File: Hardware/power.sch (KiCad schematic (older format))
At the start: 0 parts

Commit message: add power jack, 3.3V regulator, VREF divider
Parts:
- added C?: 220uF, symbol CP1_Small
- added C?: 1uF, symbol CP1_Small
- added C?: 4.7uuF, symbol CP1_Small
- added D?: D, symbol D
- added J?: Barrel_Jack, symbol Barrel_Jack
- added R? (x2): 100k, symbol R
- added U?: LD1117S33CTR, digikey-footprints:SOT-223, symbol LD1117S33CTR
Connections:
- new net: D?.2 (A), J?.1
- new net +15V: C?.1, D?.1 (K), R?.1, U?.3 (VIN)
- new net +3V3: C?.1, U?.2 (VOUT), U?.4 (VOUT)
- new net GND: C?.2, C?.2, C?.2, J?.2, R?.2, U?.1 (GND)
- new net VREF: C?.1, R?.1, R?.2
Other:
- note added: "Check wall wart \npolarity vs DC barrel \njack pinout"

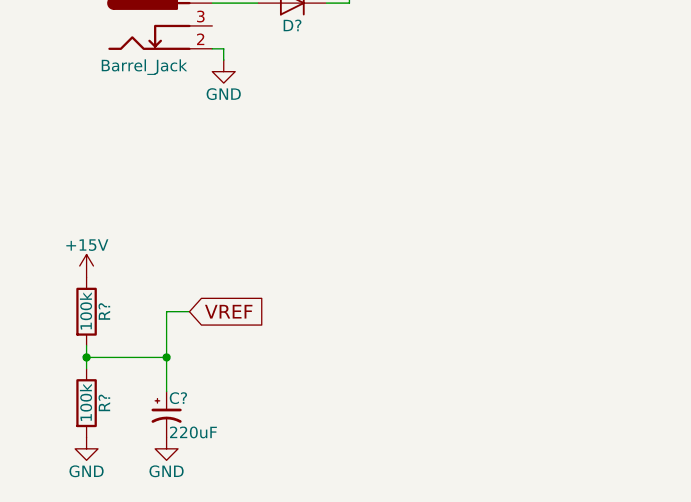
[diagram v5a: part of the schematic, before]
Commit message: add VREF to all single supply op amps
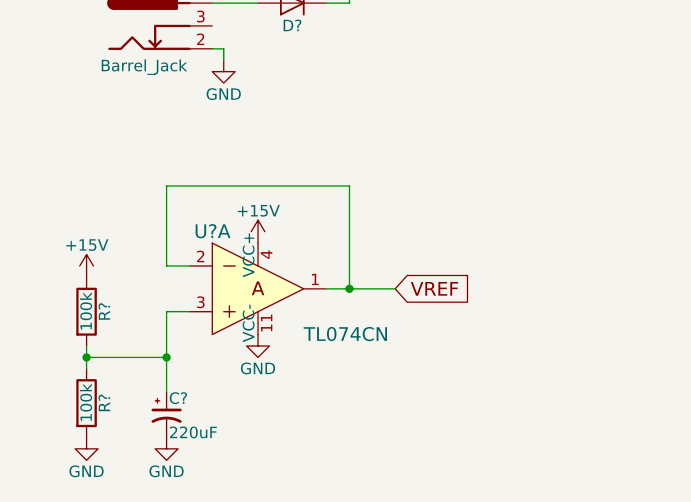
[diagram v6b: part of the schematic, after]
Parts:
- added U?: TL074CN, digikey-footprints:DIP-14_W3mm, symbol TL074CN
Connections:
- net +15V: now also U?.4 (VCC+)
- net GND: now also U?.11 (VCC-)
- net VREF: now also U?.1, U?.2; no longer C?.1, R?.1, R?.2
- new net: C?.1, R?.1, R?.2, U?.3
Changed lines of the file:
@@
 $Descr A4 11693 8268
 encoding utf-8
-Sheet 3 8
+Sheet 3 7
 Title ""
 Date ""
@@
 $EndComp
 Wire Wire Line
-	1550 3200 1550 3100
+	1550 3100 1550 3200
 Wire Wire Line
 	1900 2950 1900 3300
@@
 	1900 3150 1550 3150
 Connection ~ 1550 3150
-Text GLabel 2000 2950 2    60   Input ~ 0
+Text GLabel 2900 2850 2    60   Input ~ 0
 VREF
 Wire Wire Line
@@
 	1    0    0    -1
 $EndComp
+$Comp
+L TL074CN U?
+U 1 1 5C39B9EB
+P 2300 2850
+F 0 "U?" H 2100 3100 60  0000 C CNN
+F 1 "TL074CN" H 2500 2650 60  0000 L CNN
+F 2 "digikey-footprints:DIP-14_W3mm" H 2500 3050 60  0001 L CNN
+F 3 "http://www.ti.com/lit/ds/symlink/tl071a.pdf" H 2500 3150 60  0001 L CNN
+F 4 "296-1777-5-ND" H 2500 3250 60  0001 L CNN "Digi-Key_PN"
+F 5 "TL074CN" H 2500 3350 60  0001 L CNN "MPN"
+F 6 "Integrated Circuits (ICs)" H 2500 3450 60  0001 L CNN "Category"
+F 7 "Linear - Amplifiers - Instrumentation, OP Amps, Buffer Amps" H 2500 3550 60  0001 L CNN "Family"
+F 8 "http://www.ti.com/lit/ds/symlink/tl071a.pdf" H 2500 3650 60  0001 L CNN "DK_Datasheet_Link"
+F 9 "/product-detail/en/texas-instruments/TL074CN/296-1777-5-ND/277423" H 2500 3750 60  0001 L CNN "DK_Detail_Page"
+F 10 "IC OPAMP JFET 3MHZ 14DIP" H 2500 3850 60  0001 L CNN "Description"
+F 11 "Texas Instruments" H 2500 3950 60  0001 L CNN "Manufacturer"
+F 12 "Active" H 2500 4050 60  0001 L CNN "Status"
+	1    2300 2850
+	1    0    0    -1
+$EndComp
+$Comp
+L GND #PWR?
+U 1 1 5C39BA81
+P 2300 3050
+F 0 "#PWR?" H 2300 2800 50  0001 C CNN
+F 1 "GND" H 2300 2900 50  0000 C CNN
+F 2 "" H 2300 3050 50  0001 C CNN
+F 3 "" H 2300 3050 50  0001 C CNN
+	1    2300 3050
+	1    0    0    -1
+$EndComp
+$Comp
+L +15V #PWR?
+U 1 1 5C39BAA7
+P 2300 2650
+F 0 "#PWR?" H 2300 2500 50  0001 C CNN
+F 1 "+15V" H 2300 2790 50  0000 C CNN
+F 2 "" H 2300 2650 50  0001 C CNN
+F 3 "" H 2300 2650 50  0001 C CNN
+	1    2300 2650
+	1    0    0    -1
+$EndComp
+Wire Wire Line
+	2600 2850 2900 2850
+Wire Wire Line
+	2700 2850 2700 2400
+Wire Wire Line
+	2700 2400 1900 2400
+Wire Wire Line
+	1900 2400 1900 2750
+Wire Wire Line
+	1900 2750 2000 2750
+Connection ~ 2700 2850
 $EndSCHEMATC

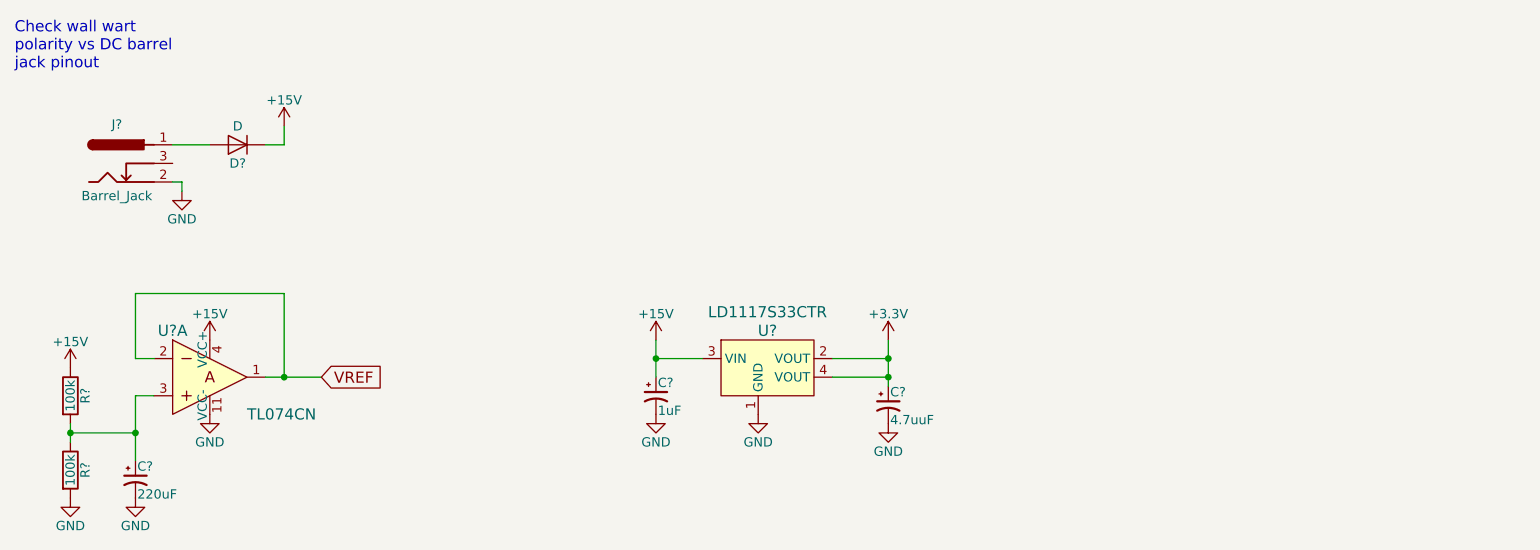
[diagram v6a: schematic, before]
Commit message: associate footprints with all components
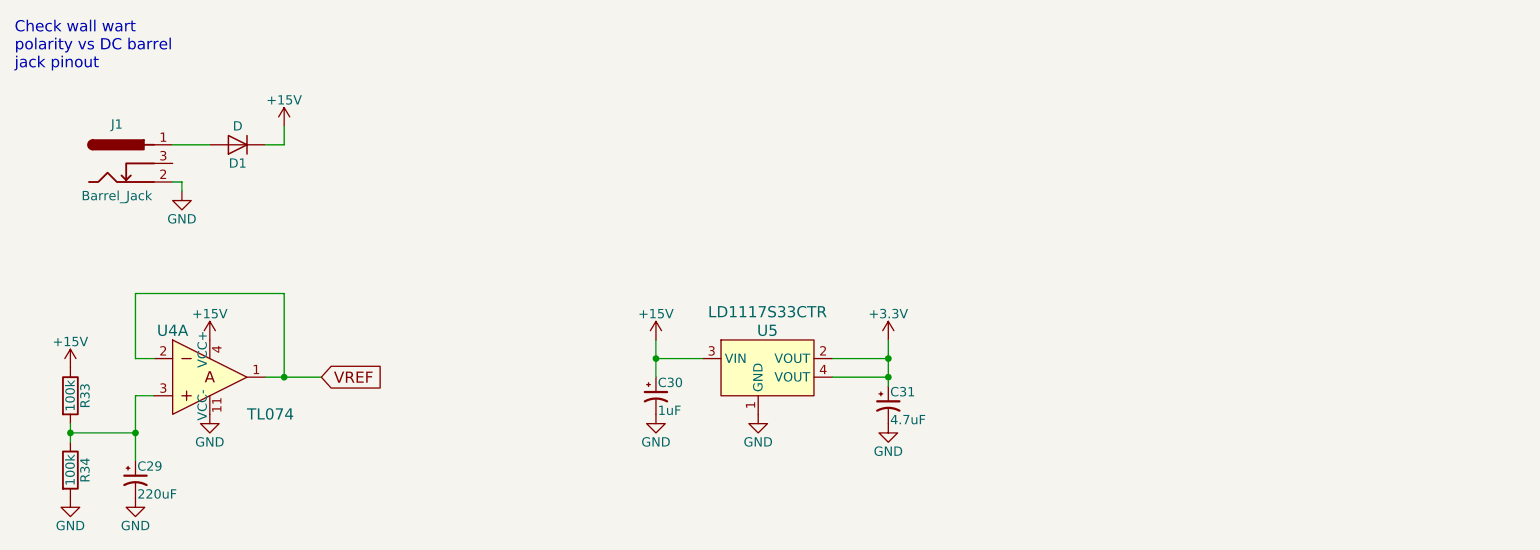
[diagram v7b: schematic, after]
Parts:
- C29: renamed from C?; footprint (none) -> Capacitors_SMD:CP_Elec_8x10
- C30: renamed from C?; footprint (none) -> Capacitors_SMD:CP_Elec_4x4.5
- C31: renamed from C?; value 4.7uuF -> 4.7uF; footprint (none) -> Capacitors_SMD:CP_Elec_4x5.7
- D1: renamed from D?; footprint (none) -> digikey-footprints:TO-252-3
- J1: renamed from J?; footprint (none) -> Connectors:BARREL_JACK
- R33, R34: renamed from R?; footprint (none) -> digikey-footprints:0805
- U4: renamed from U?; value TL074CN -> TL074; footprint digikey-footprints:DIP-14_W3mm -> digikey-footprints:SOIC-14_W3.9mm
- gave numbers to parts that had none: 1
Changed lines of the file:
@@
 $EndDescr
 $Comp
-L Barrel_Jack J?
+L Barrel_Jack J1
 U 1 1 5C392266
 P 1800 1700
-F 0 "J?" H 1800 1910 50  0000 C CNN
+F 0 "J1" H 1800 1910 50  0000 C CNN
 F 1 "Barrel_Jack" H 1800 1525 50  0000 C CNN
-F 2 "" H 1850 1660 50  0001 C CNN
+F 2 "Connectors:BARREL_JACK" H 1850 1660 50  0001 C CNN
 F 3 "" H 1850 1660 50  0001 C CNN
 	1    1800 1700
@@
 $EndComp
 $Comp
-L +15V #PWR?
+L +15V #PWR037
 U 1 1 5C3922F5
 P 2700 1500
-F 0 "#PWR?" H 2700 1350 50  0001 C CNN
+F 0 "#PWR037" H 2700 1350 50  0001 C CNN
 F 1 "+15V" H 2700 1640 50  0000 C CNN
 F 2 "" H 2700 1500 50  0001 C CNN
@@
 Check wall wart \npolarity vs DC barrel \njack pinout
 $Comp
-L GND #PWR?
+L GND #PWR038
 U 1 1 5C39231B
 P 2150 1850
-F 0 "#PWR?" H 2150 1600 50  0001 C CNN
+F 0 "#PWR038" H 2150 1600 50  0001 C CNN
 F 1 "GND" H 2150 1700 50  0000 C CNN
 F 2 "" H 2150 1850 50  0001 C CNN
@@
 	2150 1800 2100 1800
 $Comp
-L D D?
+L D D1
 U 1 1 5C392341
 P 2450 1600
-F 0 "D?" H 2450 1700 50  0000 C CNN
+F 0 "D1" H 2450 1700 50  0000 C CNN
 F 1 "D" H 2450 1500 50  0000 C CNN
-F 2 "" H 2450 1600 50  0001 C CNN
+F 2 "digikey-footprints:TO-252-3" H 2450 1600 50  0001 C CNN
 F 3 "" H 2450 1600 50  0001 C CNN
 	1    2450 1600
@@
 	2700 1600 2600 1600
 $Comp
-L R R?
+L R R33
 U 1 1 5C3923A0
 P 1550 2950
-F 0 "R?" V 1630 2950 50  0000 C CNN
+F 0 "R33" V 1630 2950 50  0000 C CNN
 F 1 "100k" V 1550 2950 50  0000 C CNN
-F 2 "" V 1480 2950 50  0001 C CNN
+F 2 "digikey-footprints:0805" V 1480 2950 50  0001 C CNN
 F 3 "" H 1550 2950 50  0001 C CNN
 	1    1550 2950
@@
 $EndComp
 $Comp
-L R R?
+L R R34
 U 1 1 5C392430
 P 1550 3350
-F 0 "R?" V 1630 3350 50  0000 C CNN
+F 0 "R34" V 1630 3350 50  0000 C CNN
 F 1 "100k" V 1550 3350 50  0000 C CNN
-F 2 "" V 1480 3350 50  0001 C CNN
+F 2 "digikey-footprints:0805" V 1480 3350 50  0001 C CNN
 F 3 "" H 1550 3350 50  0001 C CNN
 	1    1550 3350
@@
 $EndComp
 $Comp
-L CP1_Small C?
+L CP1_Small C29
 U 1 1 5C392458
 P 1900 3400
-F 0 "C?" H 1910 3470 50  0000 L CNN
+F 0 "C29" H 1910 3470 50  0000 L CNN
 F 1 "220uF" H 1910 3320 50  0000 L CNN
-F 2 "" H 1900 3400 50  0001 C CNN
+F 2 "Capacitors_SMD:CP_Elec_8x10" H 1900 3400 50  0001 C CNN
 F 3 "" H 1900 3400 50  0001 C CNN
 	1    1900 3400
@@
 $EndComp
 $Comp
-L GND #PWR?
+L GND #PWR039
 U 1 1 5C392477
 P 1550 3500
-F 0 "#PWR?" H 1550 3250 50  0001 C CNN
+F 0 "#PWR039" H 1550 3250 50  0001 C CNN
 F 1 "GND" H 1550 3350 50  0000 C CNN
 F 2 "" H 1550 3500 50  0001 C CNN
@@
 $EndComp
 $Comp
-L GND #PWR?
+L GND #PWR040
 U 1 1 5C392498
 P 1900 3500
-F 0 "#PWR?" H 1900 3250 50  0001 C CNN
+F 0 "#PWR040" H 1900 3250 50  0001 C CNN
 F 1 "GND" H 1900 3350 50  0000 C CNN
 F 2 "" H 1900 3500 50  0001 C CNN
@@
 $EndComp
 $Comp
-L +15V #PWR?
+L +15V #PWR041
 U 1 1 5C3924B7
 P 1550 2800
-F 0 "#PWR?" H 1550 2650 50  0001 C CNN
+F 0 "#PWR041" H 1550 2650 50  0001 C CNN
 F 1 "+15V" H 1550 2940 50  0000 C CNN
 F 2 "" H 1550 2800 50  0001 C CNN
@@
 Connection ~ 1900 3150
 $Comp
-L LD1117S33CTR U?
+L LD1117S33CTR U5
 U 1 1 5C392D20
 P 5250 2750
-F 0 "U?" H 5300 2900 60  0000 C CNN
+F 0 "U5" H 5300 2900 60  0000 C CNN
 F 1 "LD1117S33CTR" H 5300 3000 60  0000 C CNN
 F 2 "digikey-footprints:SOT-223" H 5450 2950 60  0001 L CNN
@@
 $EndComp
 $Comp
-L CP1_Small C?
+L CP1_Small C30
 U 1 1 5C392DFE
 P 4700 2950
-F 0 "C?" H 4710 3020 50  0000 L CNN
+F 0 "C30" H 4710 3020 50  0000 L CNN
 F 1 "1uF" H 4710 2870 50  0000 L CNN
-F 2 "" H 4700 2950 50  0001 C CNN
+F 2 "Capacitors_SMD:CP_Elec_4x4.5" H 4700 2950 50  0001 C CNN
 F 3 "" H 4700 2950 50  0001 C CNN
 	1    4700 2950
@@
 	4700 2750 4950 2750
 $Comp
-L +15V #PWR?
+L +15V #PWR042
 U 1 1 5C392EAE
 P 4700 2650
-F 0 "#PWR?" H 4700 2500 50  0001 C CNN
+F 0 "#PWR042" H 4700 2500 50  0001 C CNN
 F 1 "+15V" H 4700 2790 50  0000 C CNN
 F 2 "" H 4700 2650 50  0001 C CNN
@@
 Connection ~ 4700 2750
 $Comp
-L GND #PWR?
+L GND #PWR043
 U 1 1 5C392EE5
 P 4700 3050
-F 0 "#PWR?" H 4700 2800 50  0001 C CNN
+F 0 "#PWR043" H 4700 2800 50  0001 C CNN
 F 1 "GND" H 4700 2900 50  0000 C CNN
 F 2 "" H 4700 3050 50  0001 C CNN
@@
 $EndComp
 $Comp
-L GND #PWR?
+L GND #PWR044
 U 1 1 5C392F13
 P 5250 3050
-F 0 "#PWR?" H 5250 2800 50  0001 C CNN
+F 0 "#PWR044" H 5250 2800 50  0001 C CNN
 F 1 "GND" H 5250 2900 50  0000 C CNN
 F 2 "" H 5250 3050 50  0001 C CNN
@@
 $EndComp
 $Comp
-L +3.3V #PWR?
+L +3.3V #PWR045
 U 1 1 5C392F35
 P 5950 2650
-F 0 "#PWR?" H 5950 2500 50  0001 C CNN
+F 0 "#PWR045" H 5950 2500 50  0001 C CNN
 F 1 "+3.3V" H 5950 2790 50  0000 C CNN
 F 2 "" H 5950 2650 50  0001 C CNN
@@
 Connection ~ 5950 2750
 $Comp
-L CP1_Small C?
+L CP1_Small C31
 U 1 1 5C392F95
 P 5950 3000
-F 0 "C?" H 5960 3070 50  0000 L CNN
-F 1 "4.7uuF" H 5960 2920 50  0000 L CNN
-F 2 "" H 5950 3000 50  0001 C CNN
+F 0 "C31" H 5960 3070 50  0000 L CNN
+F 1 "4.7uF" H 5960 2920 50  0000 L CNN
+F 2 "Capacitors_SMD:CP_Elec_4x5.7" H 5950 3000 50  0001 C CNN
 F 3 "" H 5950 3000 50  0001 C CNN
 	1    5950 3000
@@
 Connection ~ 5950 2850
 $Comp
-L GND #PWR?
+L GND #PWR046
 U 1 1 5C393000
 P 5950 3100
-F 0 "#PWR?" H 5950 2850 50  0001 C CNN
+F 0 "#PWR046" H 5950 2850 50  0001 C CNN
 F 1 "GND" H 5950 2950 50  0000 C CNN
 F 2 "" H 5950 3100 50  0001 C CNN
@@
 $EndComp
 $Comp
-L TL074CN U?
+L GND #PWR047
+U 1 1 5C39BA81
+P 2300 3050
+F 0 "#PWR047" H 2300 2800 50  0001 C CNN
+F 1 "GND" H 2300 2900 50  0000 C CNN
+F 2 "" H 2300 3050 50  0001 C CNN
+F 3 "" H 2300 3050 50  0001 C CNN
+	1    2300 3050
+	1    0    0    -1
+$EndComp
+$Comp
+L +15V #PWR048
+U 1 1 5C39BAA7
+P 2300 2650
+F 0 "#PWR048" H 2300 2500 50  0001 C CNN
+F 1 "+15V" H 2300 2790 50  0000 C CNN
+F 2 "" H 2300 2650 50  0001 C CNN
+F 3 "" H 2300 2650 50  0001 C CNN
+	1    2300 2650
+	1    0    0    -1
+$EndComp
+Wire Wire Line
+	2600 2850 2900 2850
+Wire Wire Line
+	2700 2850 2700 2400
+Wire Wire Line
+	2700 2400 1900 2400
+Wire Wire Line
+	1900 2400 1900 2750
+Wire Wire Line
+	1900 2750 2000 2750
+Connection ~ 2700 2850
+$Comp
+L TL074CN U4
 U 1 1 5C39B9EB
 P 2300 2850
-F 0 "U?" H 2100 3100 60  0000 C CNN
-F 1 "TL074CN" H 2500 2650 60  0000 L CNN
-F 2 "digikey-footprints:DIP-14_W3mm" H 2500 3050 60  0001 L CNN
+F 0 "U4" H 2100 3100 60  0000 C CNN
+F 1 "TL074" H 2500 2650 60  0000 L CNN
+F 2 "digikey-footprints:SOIC-14_W3.9mm" H 2500 3050 60  0001 L CNN
 F 3 "http://www.ti.com/lit/ds/symlink/tl071a.pdf" H 2500 3150 60  0001 L CNN
 F 4 "296-1777-5-ND" H 2500 3250 60  0001 L CNN "Digi-Key_PN"
@@
 	1    0    0    -1
 $EndComp
-$Comp
-L GND #PWR?
-U 1 1 5C39BA81
-P 2300 3050
-F 0 "#PWR?" H 2300 2800 50  0001 C CNN
-F 1 "GND" H 2300 2900 50  0000 C CNN
-F 2 "" H 2300 3050 50  0001 C CNN
-F 3 "" H 2300 3050 50  0001 C CNN
-	1    2300 3050
-	1    0    0    -1
-$EndComp
-$Comp
-L +15V #PWR?
-U 1 1 5C39BAA7
-P 2300 2650
-F 0 "#PWR?" H 2300 2500 50  0001 C CNN
-F 1 "+15V" H 2300 2790 50  0000 C CNN
-F 2 "" H 2300 2650 50  0001 C CNN
-F 3 "" H 2300 2650 50  0001 C CNN
-	1    2300 2650
-	1    0    0    -1
-$EndComp
-Wire Wire Line
-	2600 2850 2900 2850
-Wire Wire Line
-	2700 2850 2700 2400
-Wire Wire Line
-	2700 2400 1900 2400
-Wire Wire Line
-	1900 2400 1900 2750
-Wire Wire Line
-	1900 2750 2000 2750
-Connection ~ 2700 2850
 $EndSCHEMATC

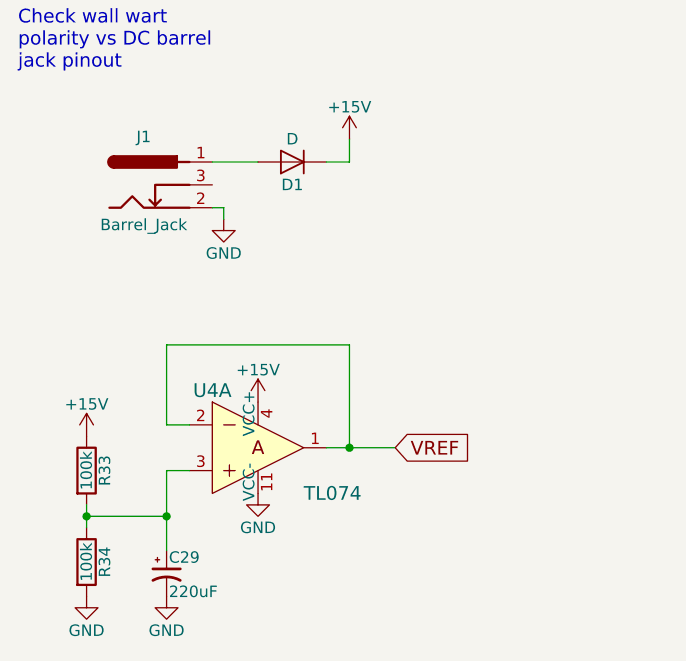
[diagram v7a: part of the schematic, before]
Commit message: fix annotation and footprints for multi-part op amps.
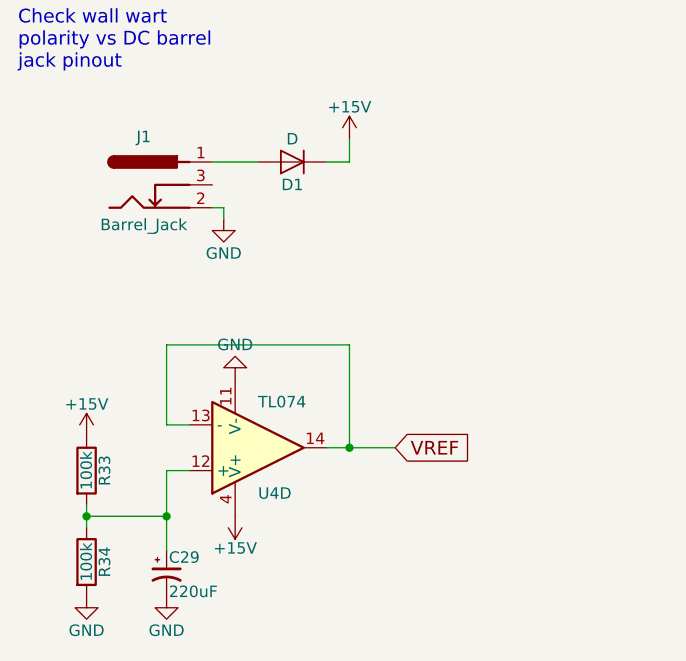
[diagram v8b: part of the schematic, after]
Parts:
- removed U4: TL074, digikey-footprints:SOIC-14_W3.9mm, symbol TL074CN
- added U4: TL074, digikey-footprints:SOIC-14_W3.9mm, symbol TL074
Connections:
- net +15V: now also U4.4 (V+)
- net GND: now also U4.11 (V-)
- net VREF: now also U4.13 (-), U4.14
- net at C29.1, R33.2, R34.1: now also U4.12 (+)
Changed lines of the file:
@@
 	1    0    0    -1
 $EndComp
-Wire Wire Line
-	2100 1600 2300 1600
 Text Notes 1250 1200 0    60   ~ 0
 Check wall wart \npolarity vs DC barrel \njack pinout
@@
 L GND #PWR047
 U 1 1 5C39BA81
-P 2300 3050
-F 0 "#PWR047" H 2300 2800 50  0001 C CNN
-F 1 "GND" H 2300 2900 50  0000 C CNN
-F 2 "" H 2300 3050 50  0001 C CNN
-F 3 "" H 2300 3050 50  0001 C CNN
-	1    2300 3050
-	1    0    0    -1
+P 2200 2550
+F 0 "#PWR047" H 2200 2300 50  0001 C CNN
+F 1 "GND" H 2200 2400 50  0000 C CNN
+F 2 "" H 2200 2550 50  0001 C CNN
+F 3 "" H 2200 2550 50  0001 C CNN
+	1    2200 2550
+	-1   0    0    1
 $EndComp
 $Comp
 L +15V #PWR048
 U 1 1 5C39BAA7
-P 2300 2650
-F 0 "#PWR048" H 2300 2500 50  0001 C CNN
-F 1 "+15V" H 2300 2790 50  0000 C CNN
-F 2 "" H 2300 2650 50  0001 C CNN
-F 3 "" H 2300 2650 50  0001 C CNN
-	1    2300 2650
-	1    0    0    -1
+P 2200 3150
+F 0 "#PWR048" H 2200 3000 50  0001 C CNN
+F 1 "+15V" H 2200 3290 50  0000 C CNN
+F 2 "" H 2200 3150 50  0001 C CNN
+F 3 "" H 2200 3150 50  0001 C CNN
+	1    2200 3150
+	-1   0    0    1
 $EndComp
 Wire Wire Line
@@
 	1900 2750 2000 2750
 Connection ~ 2700 2850
-$Comp
-L TL074CN U4
-U 1 1 5C39B9EB
+Wire Wire Line
+	2300 1600 2100 1600
+$Comp
+L TL074 U4
+U 4 1 5C3D82DF
 P 2300 2850
-F 0 "U4" H 2100 3100 60  0000 C CNN
-F 1 "TL074" H 2500 2650 60  0000 L CNN
-F 2 "digikey-footprints:SOIC-14_W3.9mm" H 2500 3050 60  0001 L CNN
-F 3 "http://www.ti.com/lit/ds/symlink/tl071a.pdf" H 2500 3150 60  0001 L CNN
-F 4 "296-1777-5-ND" H 2500 3250 60  0001 L CNN "Digi-Key_PN"
-F 5 "TL074CN" H 2500 3350 60  0001 L CNN "MPN"
-F 6 "Integrated Circuits (ICs)" H 2500 3450 60  0001 L CNN "Category"
-F 7 "Linear - Amplifiers - Instrumentation, OP Amps, Buffer Amps" H 2500 3550 60  0001 L CNN "Family"
-F 8 "http://www.ti.com/lit/ds/symlink/tl071a.pdf" H 2500 3650 60  0001 L CNN "DK_Datasheet_Link"
-F 9 "/product-detail/en/texas-instruments/TL074CN/296-1777-5-ND/277423" H 2500 3750 60  0001 L CNN "DK_Detail_Page"
-F 10 "IC OPAMP JFET 3MHZ 14DIP" H 2500 3850 60  0001 L CNN "Description"
-F 11 "Texas Instruments" H 2500 3950 60  0001 L CNN "Manufacturer"
-F 12 "Active" H 2500 4050 60  0001 L CNN "Status"
-	1    2300 2850
-	1    0    0    -1
+F 0 "U4" H 2300 3050 50  0000 L CNN
+F 1 "TL074" H 2300 2650 50  0000 L CNN
+F 2 "digikey-footprints:SOIC-14_W3.9mm" H 2250 2950 50  0001 C CNN
+F 3 "" H 2350 3050 50  0001 C CNN
+	4    2300 2850
+	1    0    0    1
 $EndComp
 $EndSCHEMATC
